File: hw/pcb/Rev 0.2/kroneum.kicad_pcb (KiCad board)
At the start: 2 copper layers, 19 parts, among them J1 USB_B_Micro, SW1 Boot_Mode_Btn, SW2 Ctrl_One_Btn, SW3 Reset_Btn, SW4 Ctrl_Ten_Btn, U1 STM32F042F4Px

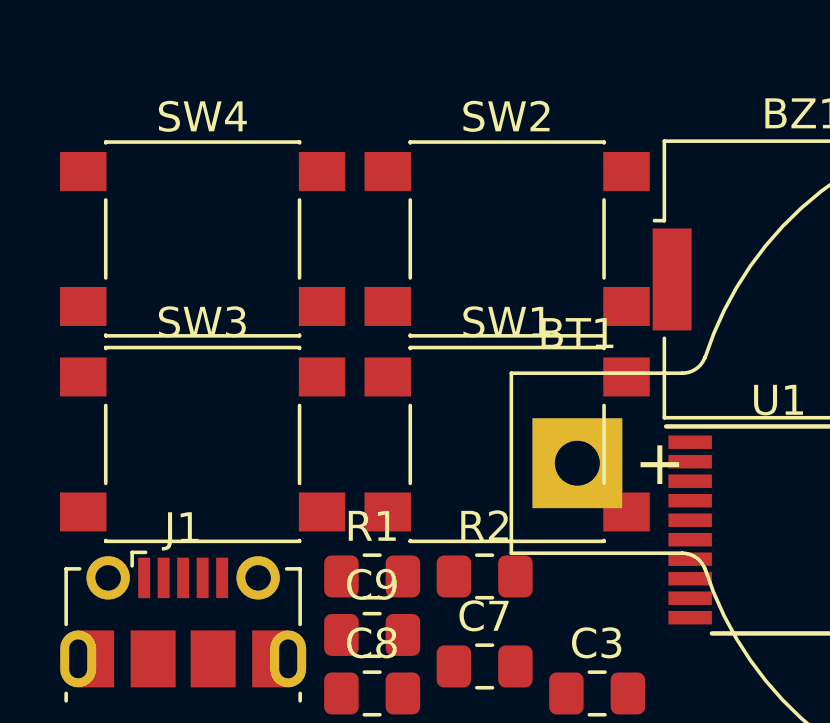
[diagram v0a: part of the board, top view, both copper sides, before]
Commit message: hw: use tl3342 for control and reset buttons.
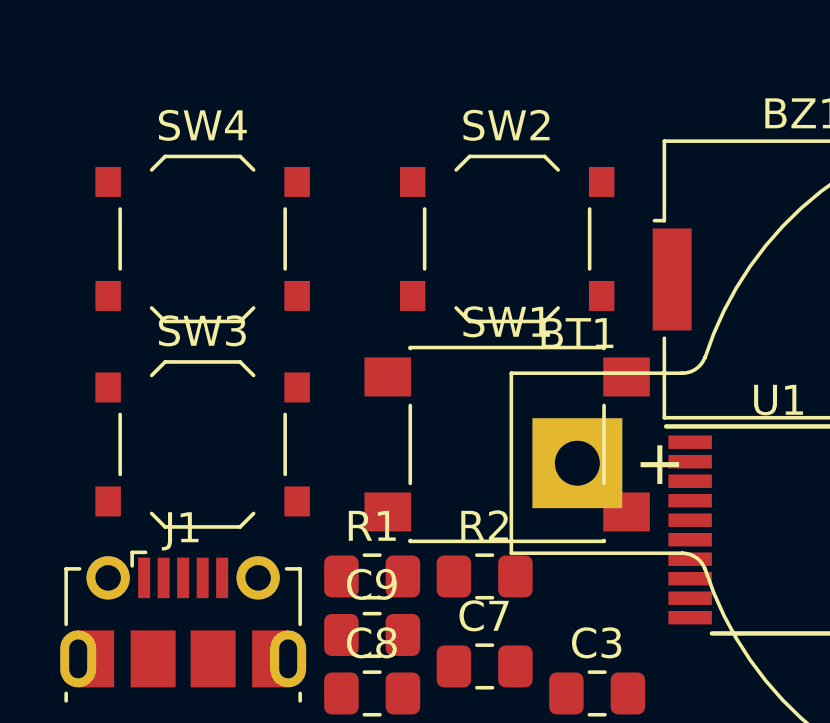
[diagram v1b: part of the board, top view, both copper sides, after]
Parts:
- SW2, SW3, SW4: footprint Button_Switch_SMD:SW_SPST_PTS645 -> tl3342:tl3342

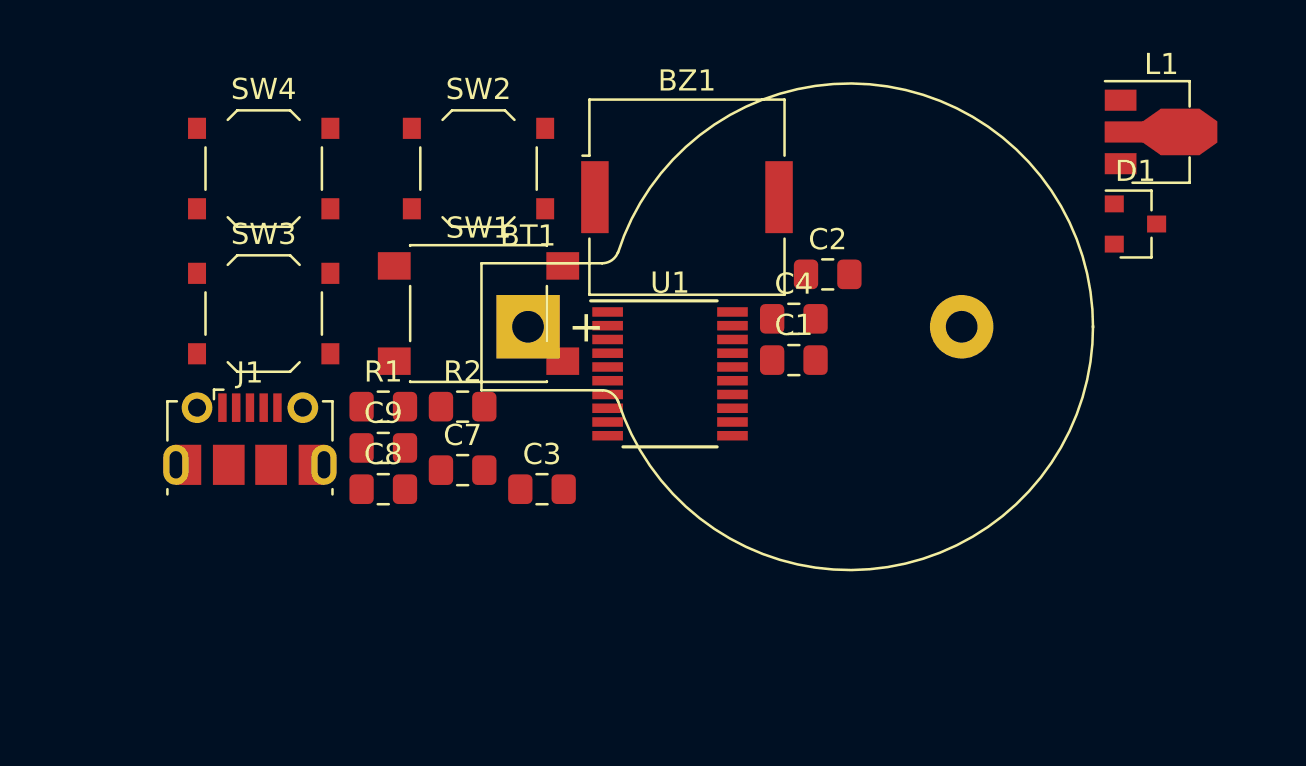
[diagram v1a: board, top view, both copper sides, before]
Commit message: hw: use momentary switch for boot mode selector.
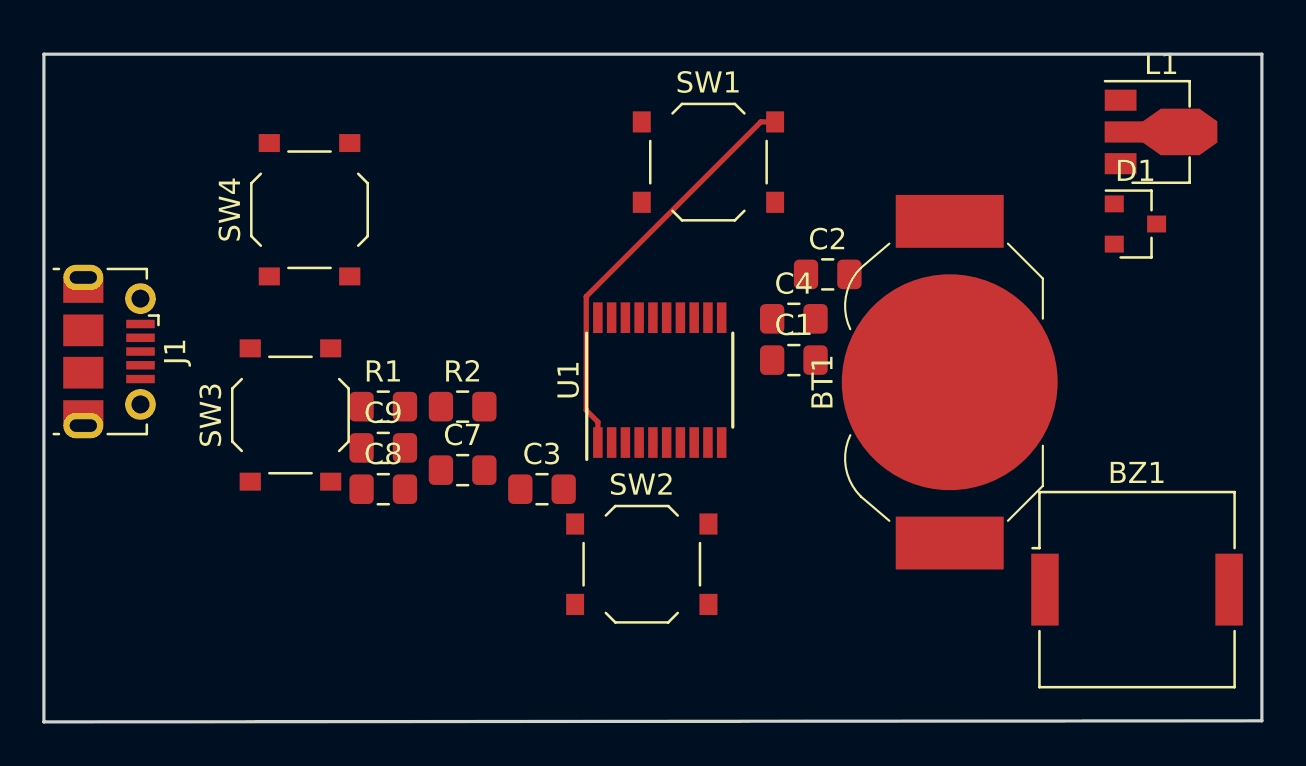
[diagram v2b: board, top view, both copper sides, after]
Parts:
- BT1: footprint Battery:BatteryHolder_Keystone_103_1x20mm -> Battery:BatteryHolder_LINX_BAT-HLD-012-SMT
- R2: value 10k -> 1M
- SW1: footprint Button_Switch_SMD:SW_SPST_PTS645 -> tl3342:tl3342
- moved BZ1 28.2 mm to (173.0, 107.6)
- moved SW2 20.2 mm to (149.6, 106.4)
- moved BT1 20.1 mm to (164.2, 97.8), turned to 270 degrees
- moved SW1 13.0 mm to (152.8, 87.4)
- moved J1 7.81 mm to (124.5, 96.3), turned to 270 degrees
- moved SW3 4.96 mm to (133.0, 99.3), turned to 90 degrees
- moved SW4 2.91 mm to (133.9, 89.7), turned to 90 degrees
- moved U1 0.57 mm to (150.4, 97.7), turned to 90 degrees
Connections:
- R2 pad 1: Net-(R2-Pad1) -> BOOT0
- R2 pad 2: BOOT0 -> GND
- SW1 pad 1: GND -> BOOT0
- SW1 pad 2: Net-(R2-Pad1) -> VDD
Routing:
- net BOOT0: track 0.00 -> 19.5 mm
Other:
- board outline added: 57.6 x 31.5 mm

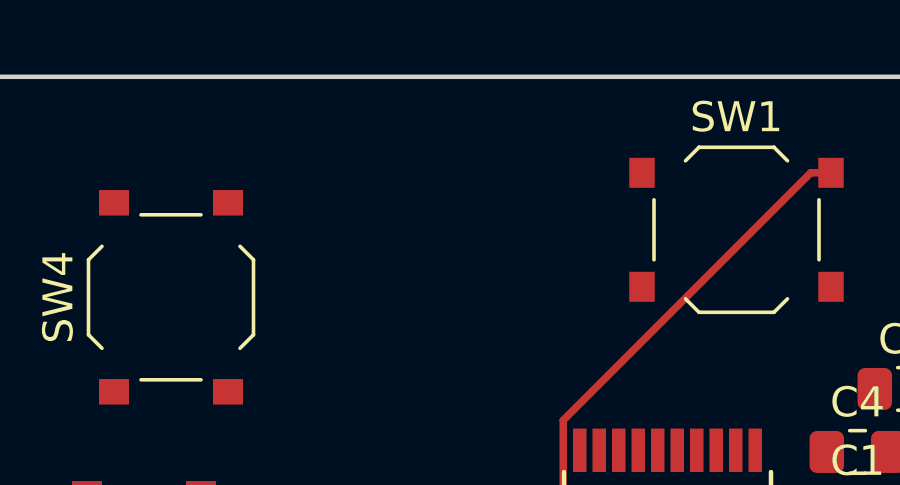
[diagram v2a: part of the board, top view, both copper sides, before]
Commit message: hw: provide footprint for SWD header.
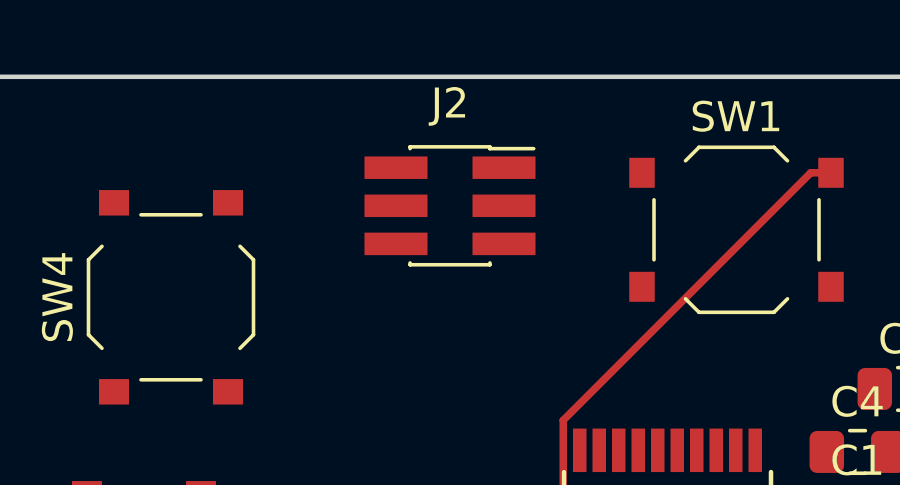
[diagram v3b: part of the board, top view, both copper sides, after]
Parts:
- added J2: SWD, Connector_PinSocket_1.27mm:PinSocket_2x03_P1.27mm_Vertical_SMD, F.Cu at (143.2, 86.6)
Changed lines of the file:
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@@
     (tracks 5)
     (zones 0)
-    (modules 19)
-    (nets 26)
+    (modules 20)
+    (nets 27)
   )
   (page A4)
@@
   (net 24 SWDIO)
   (net 25 SWCLK)
+  (net 26 "Net-(J2-Pad6)")
   (net_class Default "This is the default net class."
     (clearance 0.2)
@@
     (add_net "Net-(J1-Pad4)")
     (add_net "Net-(J1-Pad6)")
+    (add_net "Net-(J2-Pad6)")
     (add_net "Net-(U1-Pad10)")
     (add_net "Net-(U1-Pad11)")
@@
       (at (xyz 0 0 0))
       (scale (xyz 1 1 1))
+      (rotate (xyz 0 0 0))
+    )
+  )
+  (module Connector_PinSocket_1.27mm:PinSocket_2x03_P1.27mm_Vertical_SMD (layer F.Cu)
+    (at 143.2 86.6)
+    (descr "surface-mounted straight socket strip, 2x03, 1.27mm pitch, double cols (from Kicad 4.0.7!), script generated")
+    (tags "Surface mounted socket strip SMD 2x03 1.27mm double row")
+    (attr smd)
+    (fp_text reference J2 (at 0 -3.405) (layer F.SilkS)
+      (effects (font (size 1 1) (thickness 0.15)))
+    )
+    (fp_text value SWD (at 0 3.405) (layer F.Fab)
+      (effects (font (size 1 1) (thickness 0.15)))
+    )
+    (fp_line (start -1.33 -1.965) (end 1.33 -1.965) (layer F.SilkS) (width 0.12))
+    (fp_line (start 1.33 -1.965) (end 1.33 -1.905) (layer F.SilkS) (width 0.12))
+    (fp_line (start 1.33 1.905) (end 1.33 1.965) (layer F.SilkS) (width 0.12))
+    (fp_line (start -1.33 1.965) (end 1.33 1.965) (layer F.SilkS) (width 0.12))
+    (fp_line (start -1.33 -1.965) (end -1.33 -1.905) (layer F.SilkS) (width 0.12))
+    (fp_line (start -1.33 1.905) (end -1.33 1.965) (layer F.SilkS) (width 0.12))
+    (fp_line (start 1.33 -1.905) (end 2.79 -1.905) (layer F.SilkS) (width 0.12))
+    (fp_line (start -1.27 -1.905) (end 0.635 -1.905) (layer F.Fab) (width 0.1))
+    (fp_line (start 0.635 -1.905) (end 1.27 -1.27) (layer F.Fab) (width 0.1))
+    (fp_line (start 1.27 -1.27) (end 1.27 1.905) (layer F.Fab) (width 0.1))
+    (fp_line (start 1.27 1.905) (end -1.27 1.905) (layer F.Fab) (width 0.1))
+    (fp_line (start -1.27 1.905) (end -1.27 -1.905) (layer F.Fab) (width 0.1))
+    (fp_line (start -2.555 -1.47) (end -1.27 -1.47) (layer F.Fab) (width 0.1))
+    (fp_line (start -1.27 -1.07) (end -2.555 -1.07) (layer F.Fab) (width 0.1))
+    (fp_line (start -2.555 -1.07) (end -2.555 -1.47) (layer F.Fab) (width 0.1))
+    (fp_line (start 1.27 -1.47) (end 2.555 -1.47) (layer F.Fab) (width 0.1))
+    (fp_line (start 2.555 -1.47) (end 2.555 -1.07) (layer F.Fab) (width 0.1))
+    (fp_line (start 2.555 -1.07) (end 1.27 -1.07) (layer F.Fab) (width 0.1))
+    (fp_line (start -2.555 -0.2) (end -1.27 -0.2) (layer F.Fab) (width 0.1))
+    (fp_line (start -1.27 0.2) (end -2.555 0.2) (layer F.Fab) (width 0.1))
+    (fp_line (start -2.555 0.2) (end -2.555 -0.2) (layer F.Fab) (width 0.1))
+    (fp_line (start 1.27 -0.2) (end 2.555 -0.2) (layer F.Fab) (width 0.1))
+    (fp_line (start 2.555 -0.2) (end 2.555 0.2) (layer F.Fab) (width 0.1))
+    (fp_line (start 2.555 0.2) (end 1.27 0.2) (layer F.Fab) (width 0.1))
+    (fp_line (start -2.555 1.07) (end -1.27 1.07) (layer F.Fab) (width 0.1))
+    (fp_line (start -1.27 1.47) (end -2.555 1.47) (layer F.Fab) (width 0.1))
+    (fp_line (start -2.555 1.47) (end -2.555 1.07) (layer F.Fab) (width 0.1))
+    (fp_line (start 1.27 1.07) (end 2.555 1.07) (layer F.Fab) (width 0.1))
+    (fp_line (start 2.555 1.07) (end 2.555 1.47) (layer F.Fab) (width 0.1))
+    (fp_line (start 2.555 1.47) (end 1.27 1.47) (layer F.Fab) (width 0.1))
+    (fp_line (start -3.35 -2.45) (end 3.35 -2.45) (layer F.CrtYd) (width 0.05))
+    (fp_line (start 3.35 -2.45) (end 3.35 2.4) (layer F.CrtYd) (width 0.05))
+    (fp_line (start 3.35 2.4) (end -3.35 2.4) (layer F.CrtYd) (width 0.05))
+    (fp_line (start -3.35 2.4) (end -3.35 -2.45) (layer F.CrtYd) (width 0.05))
+    (fp_text user %R (at 0 0 90) (layer F.Fab)
+      (effects (font (size 1 1) (thickness 0.15)))
+    )
+    (pad 1 smd rect (at 1.8 -1.27) (size 2.1 0.75) (layers F.Cu F.Paste F.Mask)
+      (net 3 VDD))
+    (pad 2 smd rect (at -1.8 -1.27) (size 2.1 0.75) (layers F.Cu F.Paste F.Mask)
+      (net 25 SWCLK))
+    (pad 3 smd rect (at 1.8 0) (size 2.1 0.75) (layers F.Cu F.Paste F.Mask)
+      (net 1 GND))
+    (pad 4 smd rect (at -1.8 0) (size 2.1 0.75) (layers F.Cu F.Paste F.Mask)
+      (net 24 SWDIO))
+    (pad 5 smd rect (at 1.8 1.27) (size 2.1 0.75) (layers F.Cu F.Paste F.Mask)
+      (net 21 NRST))
+    (pad 6 smd rect (at -1.8 1.27) (size 2.1 0.75) (layers F.Cu F.Paste F.Mask)
+      (net 26 "Net-(J2-Pad6)"))
+    (model ${KISYS3DMOD}/Connector_PinSocket_1.27mm.3dshapes/PinSocket_2x03_P1.27mm_Vertical_SMD.wrl
+      (at (xyz 0 0 0))
+      (scale (xyz 1 1 1))

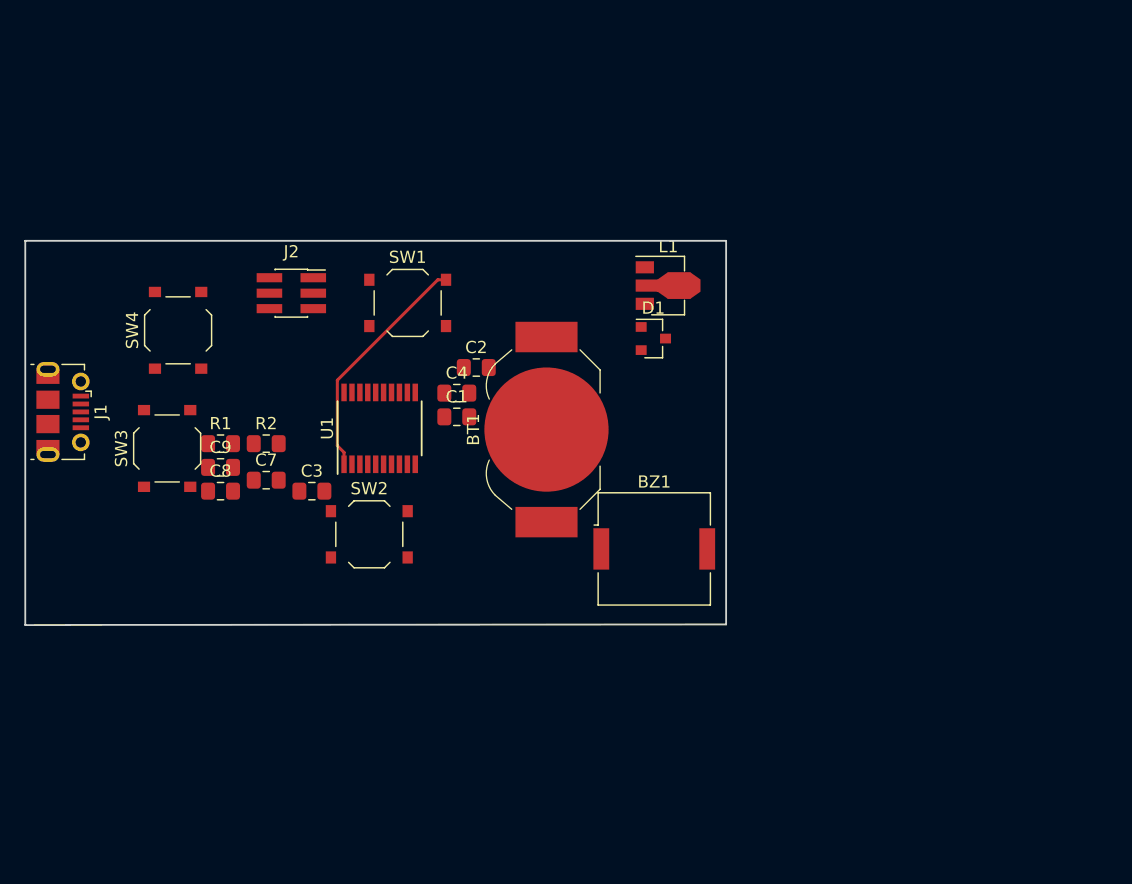
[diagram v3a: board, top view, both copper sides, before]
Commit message: hw: reorganize headers on PCB.
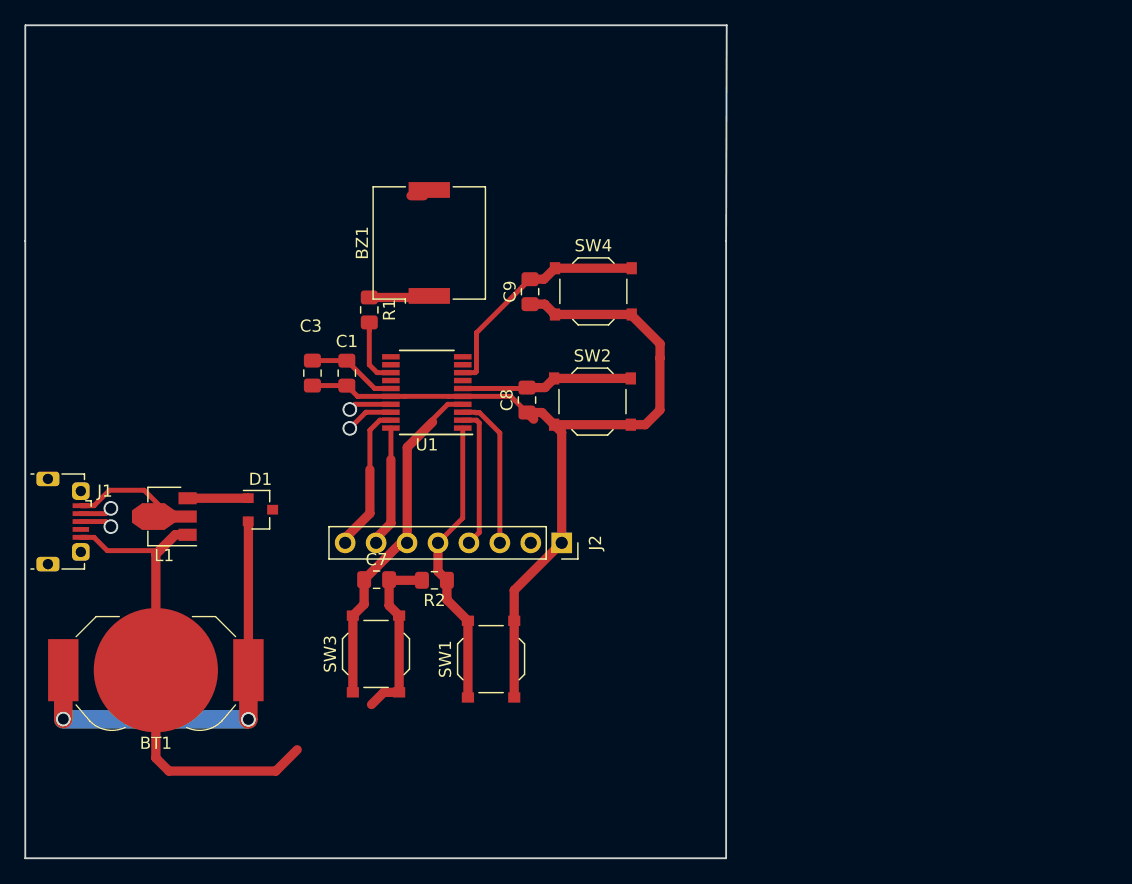
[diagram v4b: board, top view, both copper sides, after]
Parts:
- removed C2: 10n, Capacitor_SMD:C_0805_2012Metric_Pad1.15x1.40mm_HandSolder
- removed C4: 1u, Capacitor_SMD:C_0805_2012Metric_Pad1.15x1.40mm_HandSolder
- J1: footprint Connector_USB:USB_Micro-B_Molex-105017-0001 -> micro_usb:USB_Micro-B_Molex-105017-0001
- J2: value SWD -> SWD_I2C_BOOT; footprint Connector_PinSocket_1.27mm:PinSocket_2x03_P1.27mm_Vertical_SMD -> Connector_PinSocket_2.54mm:PinSocket_1x08_P2.54mm_Vertical
- moved L1 44.7 mm to (133.2, 104.9), turned to 180 degrees
- moved BT1 37.7 mm to (132.1, 117.6), turned to 0 degrees
- moved D1 35.2 mm to (140.7, 104.4)
- moved SW4 34.2 mm to (168.0, 86.5), turned to 0 degrees
- moved BZ1 31.2 mm to (154.5, 82.5), turned to 90 degrees
- moved J2 30.2 mm to (165.4, 107.1), turned to 270 degrees
- moved SW1 30.0 mm to (159.6, 116.7), turned to 90 degrees
- moved C9 29.2 mm to (162.8, 86.5), turned to 90 degrees
- moved C8 26.3 mm to (162.6, 95.4), turned to 90 degrees
- moved SW3 24.1 mm to (150.2, 116.2)
- moved SW2 21.3 mm to (167.9, 95.5)
- moved R2 17.8 mm to (154.9, 110.2), turned to 180 degrees
- moved R1 16.4 mm to (149.6, 88.0), turned to 270 degrees
- moved C7 12.2 mm to (150.2, 110.1)
- moved C1 9.72 mm to (147.8, 93.2), turned to 90 degrees
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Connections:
- J2 pad 2: SWCLK -> GND
- J2 pad 3: GND -> SCL
- J2 pad 4: SWDIO -> SDA
- J2 pad 5: NRST -> BOOT0
- J2 pad 6: Net-(J2-Pad6) -> NRST
- U1 pad 2: Net-(U1-Pad2) -> SDA
- U1 pad 3: Net-(U1-Pad3) -> SCL
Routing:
- net VDD: track 0.00 -> 73.0 mm
- net GND: track 0.00 -> 68.0 mm
- net Net-(BT1-Pad1): track 0.00 -> 35.5 mm, vias 0 -> 2
- net NRST: track 0.00 -> 28.1 mm
- net Ctrl_Ten: track 0.00 -> 19.3 mm
- net Ctrl_One: track 0.00 -> 14.1 mm
- net USB_VBUS: track 0.00 -> 13.8 mm
- net SCL: track 0.00 -> 12.8 mm
- net SDA: track 0.00 -> 11.8 mm
- net SWDIO: track 0.00 -> 11.8 mm
- net SWCLK: track 0.00 -> 9.52 mm
- net USB_D+: track 0.00 -> 6.57 mm, vias 0 -> 2
- net USB_D-: track 0.00 -> 6.20 mm, vias 0 -> 2
- net Buzzer: track 0.00 -> 5.52 mm
- net Net-(D1-Pad1): track 0.00 -> 4.98 mm
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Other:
- board size 57.6 x 31.5 mm -> 57.6 x 68.4 mm

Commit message: hw: more work on PCB.
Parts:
- moved R1 36.4 mm to (186.0, 88.6)
- moved SW4 36.4 mm to (204.4, 87.0)
- moved BZ1 36.4 mm to (190.9, 83.1)
- moved C8 36.4 mm to (198.9, 96.0)
- moved C9 36.4 mm to (199.2, 87.1)
- moved SW2 36.4 mm to (204.3, 96.1)
- moved C7 29.8 mm to (179.6, 115.1)
- moved R2 29.8 mm to (184.3, 115.2)
- moved SW1 29.8 mm to (189.0, 121.7)
- moved SW3 29.8 mm to (179.5, 121.2)
- moved J2 18.6 mm to (147.0, 104.4), turned to 0 degrees
- moved U1 13.8 mm to (160.2, 107.2)
- moved C1 13.8 mm to (153.6, 105.6)
- moved C3 13.8 mm to (150.8, 105.6)
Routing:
- net NRST: track 28.1 -> 13.0 mm
- net BOOT0: track 24.0 -> 11.4 mm
- net GND: track 68.0 -> 79.6 mm
- net SDA: track 11.8 -> 1.27 mm
- net SWDIO: track 11.8 -> 2.07 mm
- net VDD: track 73.0 -> 63.8 mm
- net SCL: track 12.8 -> 3.75 mm
- net SWCLK: track 9.52 -> 2.58 mm
